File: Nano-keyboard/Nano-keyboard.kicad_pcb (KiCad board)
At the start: 2 copper layers, 120 x 77 mm, 42 parts, among them J1 125SH-B-04-TS, J2 125SH-B-02-TS, U1 AMS1117, U2 ESP32-WROOM-32, U3 J5019, U5 EN12-HN22AF25, U6 EN12-HN22AF25

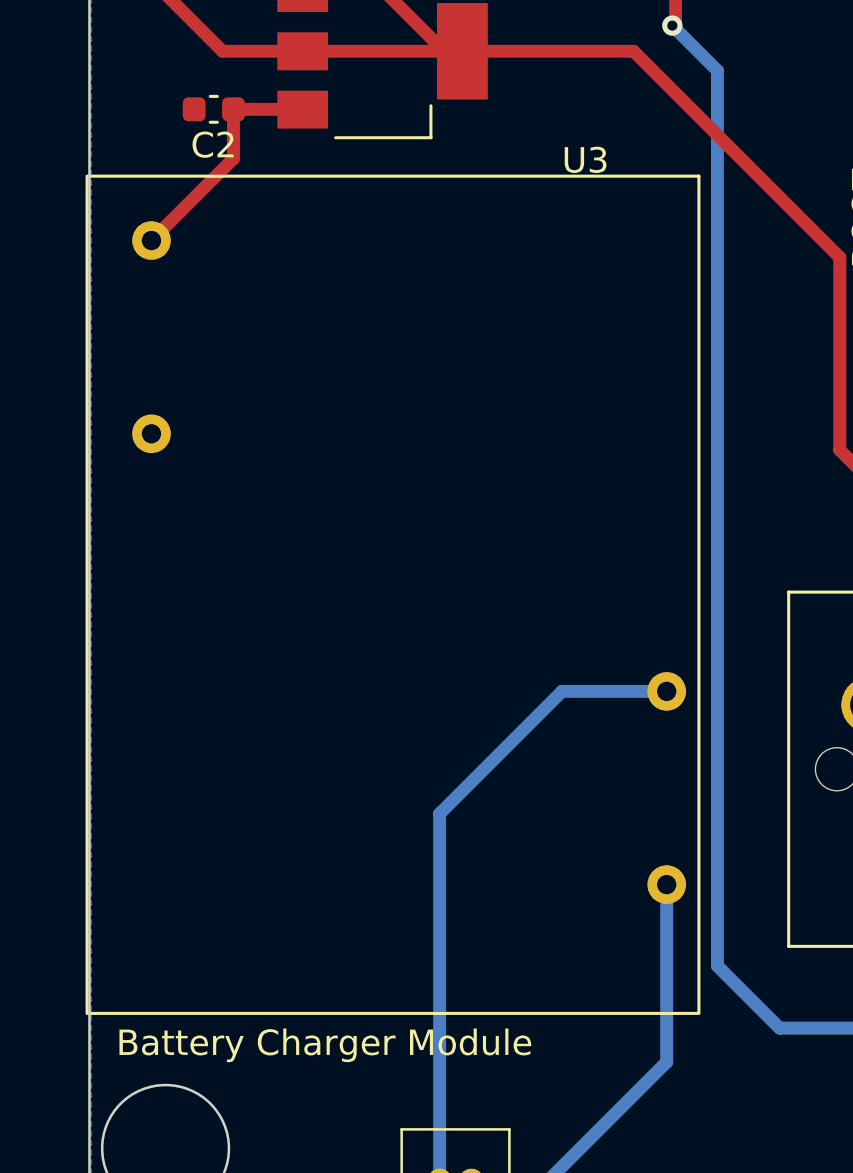
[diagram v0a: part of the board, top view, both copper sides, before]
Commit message: Footprint adjustmetns
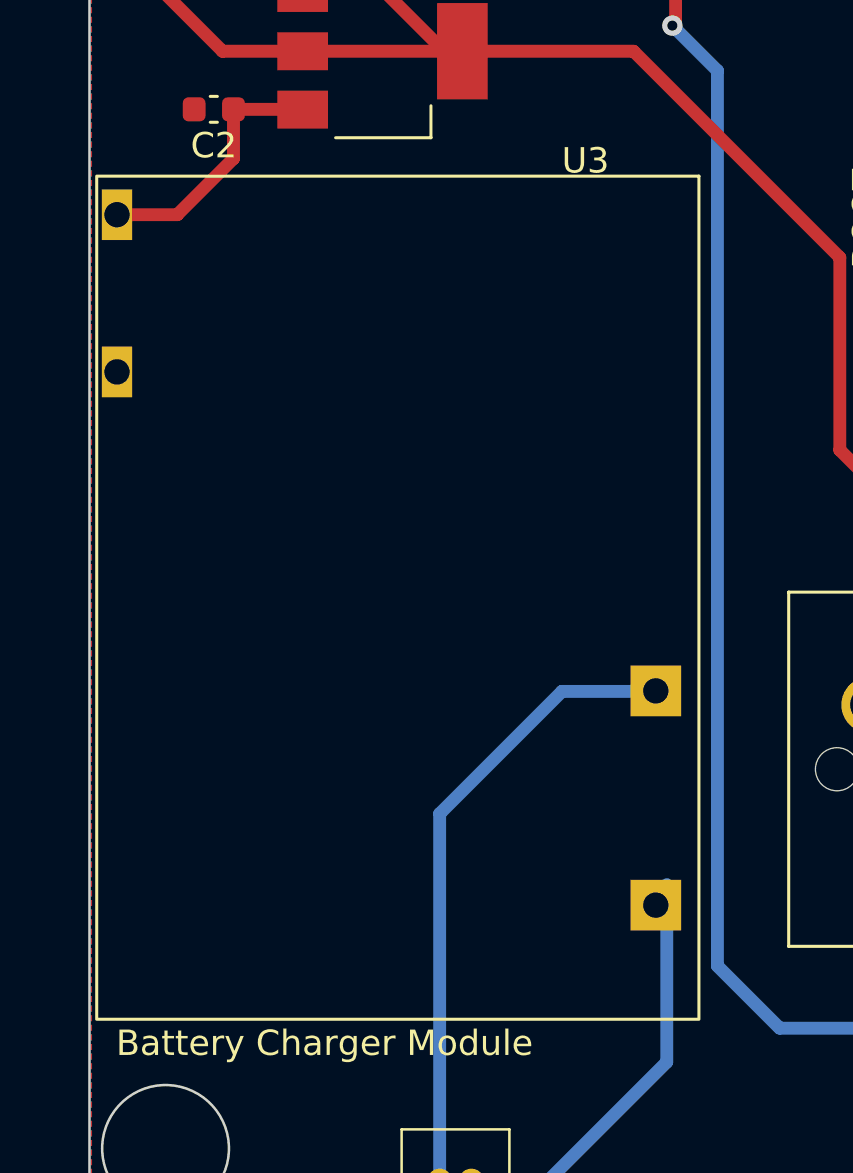
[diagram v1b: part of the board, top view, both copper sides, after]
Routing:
- net Net-(C2-Pad1): track 9.25 -> 10.2 mm
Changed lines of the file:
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@@
       (effects (font (size 1 1) (thickness 0.15)))
     )
-    (fp_rect (start 0 0) (end 33.02 24.13) (layer "F.SilkS") (width 0.12) (fill none))
-    (pad "1" thru_hole circle (at 20.32 1.27 270) (size 1.524 1.524) (drill 0.762) (layers *.Cu *.Mask)
+    (fp_rect (start 0 0) (end 33.25 23.75) (layer "F.SilkS") (width 0.12) (fill none))
+    (pad "1" thru_hole rect (at 20.3 1.7 270) (size 2 2) (drill 1) (layers *.Cu *.Mask)
       (net 49 "Net-(J2-Pad1)") (pinfunction "BAT+") (pintype "input"))
-    (pad "2" thru_hole circle (at 27.94 1.27 270) (size 1.524 1.524) (drill 0.762) (layers *.Cu *.Mask)
+    (pad "2" thru_hole rect (at 28.75 1.7 270) (size 2 2) (drill 1) (layers *.Cu *.Mask)
       (net 50 "Net-(J2-Pad2)") (pinfunction "BAT-") (pintype "input"))
-    (pad "3" thru_hole circle (at 2.54 21.59 270) (size 1.524 1.524) (drill 0.762) (layers *.Cu *.Mask)
+    (pad "3" thru_hole rect (at 1.52 22.95 270) (size 2 1.2) (drill 1) (layers *.Cu *.Mask)
       (net 43 "Net-(C2-Pad1)") (pinfunction "VOUT+") (pintype "input"))
-    (pad "4" thru_hole circle (at 10.16 21.59 270) (size 1.524 1.524) (drill 0.762) (layers *.Cu *.Mask)
+    (pad "4" thru_hole rect (at 7.72 22.95 270) (size 2 1.2) (drill 1) (layers *.Cu *.Mask)
       (net 1 "GND") (pinfunction "VOUT-") (pintype "input"))
+    (zone (net 0) (net_name "") (layer "F.Cu") (name "Keep out Module") (hatch full 0.508)
+      (connect_pads (clearance 0))
+      (min_thickness 0.254)
+      (keepout (tracks allowed) (vias not_allowed) (pads not_allowed ) (copperpour not_allowed) (footprints not_allowed))
+      (fill (thermal_gap 0.508) (thermal_bridge_width 0.508))
+      (polygon
+        (pts
+          (xy 66.96 133.675)
+          (xy 66.988006 111.119522)
+          (xy 68.89336 111.134836)
+          (xy 68.865354 105.762314)
+          (xy 66.961 105.759)
+          (xy 66.96 100.425)
+          (xy 90.71 100.425)
+          (xy 90.71 133.675)
+        )
+      )
+    )
   )
   (footprint "lib:SW_Cherry_MX_1.00u_PCB" (layer "F.Cu")
@@
   (segment (start 87.884 89.662) (end 90.678 86.868) (width 0.508) (layer "B.Cu") (net 31))
   (segment (start 130.302 82.55) (end 130.302 77.978) (width 0.508) (layer "B.Cu") (net 31))
-  (segment (start 72.353 99.732) (end 69.12 102.965) (width 0.508) (layer "F.Cu") (net 43))
   (segment (start 72.353 97.79) (end 75.072 97.79) (width 0.508) (layer "F.Cu") (net 43))
+  (segment (start 70.14 101.945) (end 72.353 99.732) (width 0.508) (layer "F.Cu") (net 43))
+  (segment (start 67.76 101.945) (end 70.14 101.945) (width 0.508) (layer "F.Cu") (net 43))
   (segment (start 72.353 97.79) (end 72.353 99.732) (width 0.508) (layer "F.Cu") (net 43))
   (segment (start 75.072 97.79) (end 75.082 97.8) (width 0.508) (layer "F.Cu") (net 43))

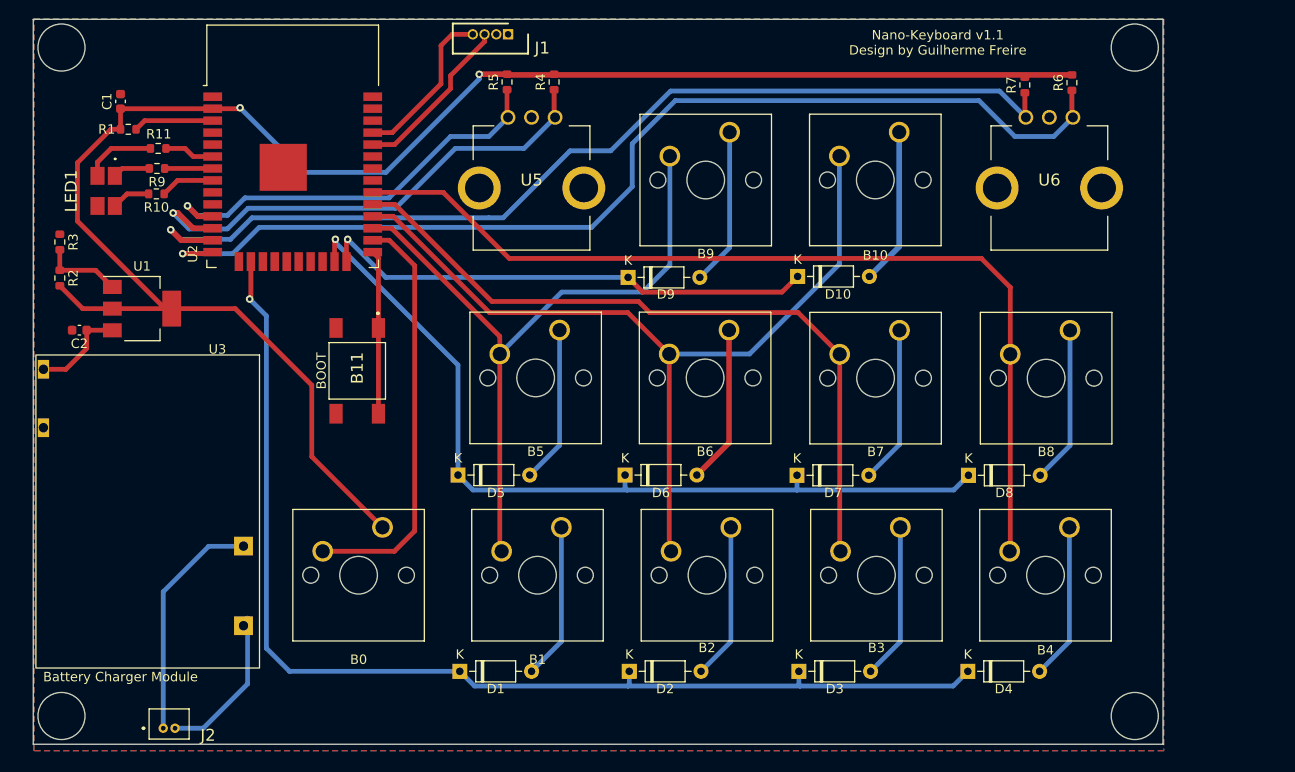
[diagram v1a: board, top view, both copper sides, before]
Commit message: Adjusting J5019 footprint
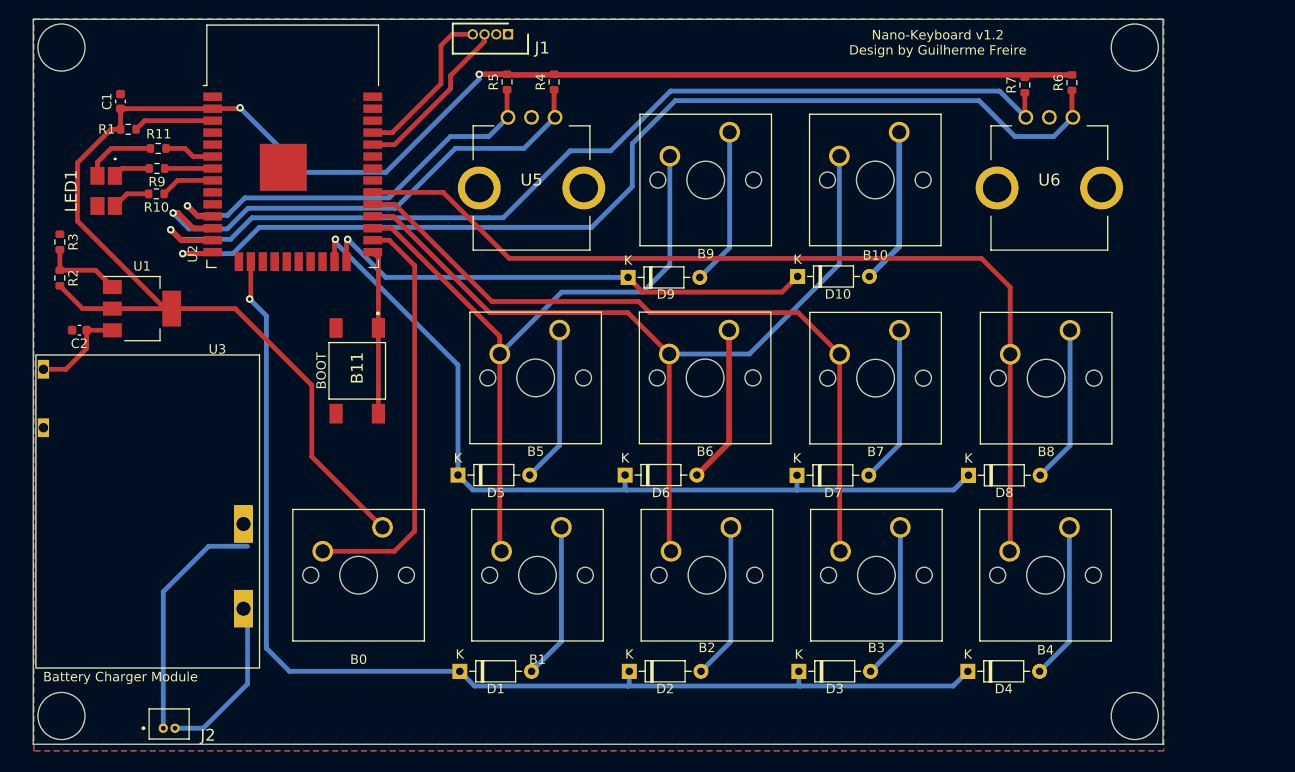
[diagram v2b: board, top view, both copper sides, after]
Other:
- board text added: "Nano-Keyboard v1.2 Design by Guilherme Freire"
- board text removed: "Nano-Keyboard v1.1 Design by Guilherme Freire"
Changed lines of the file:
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@@
     )
     (fp_rect (start 0 0) (end 33.25 23.75) (layer "F.SilkS") (width 0.12) (fill none))
-    (pad "1" thru_hole rect (at 20.3 1.7 270) (size 2 2) (drill 1) (layers *.Cu *.Mask)
+    (pad "1" thru_hole rect (at 17.95 1.7 270) (size 4 2) (drill 1.5) (layers *.Cu *.Mask)
       (net 49 "Net-(J2-Pad1)") (pinfunction "BAT+") (pintype "input"))
-    (pad "2" thru_hole rect (at 28.75 1.7 270) (size 2 2) (drill 1) (layers *.Cu *.Mask)
+    (pad "2" thru_hole rect (at 26.95 1.7 270) (size 4 2) (drill 1.5) (layers *.Cu *.Mask)
       (net 50 "Net-(J2-Pad2)") (pinfunction "BAT-") (pintype "input"))
     (pad "3" thru_hole rect (at 1.52 22.95 270) (size 2 1.2) (drill 1) (layers *.Cu *.Mask)
@@
           (xy 66.96 133.675)
           (xy 66.988006 111.119522)
-          (xy 68.89336 111.134836)
-          (xy 68.865354 105.762314)
+          (xy 66.980465 111.144809)
+          (xy 66.952459 105.772287)
           (xy 66.961 105.759)
           (xy 66.96 100.425)
@@
     (effects (font (size 1 1) (thickness 0.15)) (justify mirror))
   )
-  (gr_text "Nano-Keyboard v1.1\nDesign by Guilherme Freire\n" (at 162.749992 67.250005) (layer "F.SilkS")
+  (gr_text "Nano-Keyboard v1.2\nDesign by Guilherme Freire\n" (at 162.749992 67.250005) (layer "F.SilkS")
     (effects (font (size 1 1) (thickness 0.2)))
   )

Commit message: Update
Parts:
- U3: moved to B.Cu
- moved U3 32.7 mm to (90.9, 133.1), turned to 90 degrees
- moved B10 12.8 mm to (160.0, 89.5), turned to 180 degrees
- moved B9 12.7 mm to (140.0, 89.5), turned to 180 degrees
- moved B8 12.1 mm to (180.0, 109.5), turned to 180 degrees
- moved B5 12.0 mm to (120.0, 109.5), turned to 180 degrees
- moved B7 11.7 mm to (160.0, 109.5), turned to 180 degrees
- moved B6 11.7 mm to (140.0, 109.5), turned to 180 degrees
- moved B0 11.4 mm to (100.0, 129.5), turned to 180 degrees
- moved B4 11.2 mm to (180.0, 129.5), turned to 180 degrees
- moved B1 11.1 mm to (120.0, 129.5), turned to 180 degrees
- moved U6 11.0 mm to (187.9, 77.1)
- moved B3 10.8 mm to (160.0, 129.5), turned to 180 degrees
- moved B2 10.8 mm to (140.0, 129.5), turned to 180 degrees
- moved D4 9.79 mm to (175.7, 133.3)
- moved D8 9.70 mm to (175.7, 113.1)
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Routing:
- net +3V3: track 186.2 -> 0.00 mm, vias 2 -> 0
- net ROW1: track 121.9 -> 0.00 mm, vias 1 -> 0
- net /ENCODER1_A: track 112.5 -> 0.00 mm, vias 1 -> 0
- net /ENCODER1_B: track 106.5 -> 0.00 mm, vias 1 -> 0
- net COL4: track 100.0 -> 0.00 mm
- net COL2: track 92.1 -> 0.00 mm
- net ROW2: track 91.7 -> 0.00 mm, vias 1 -> 0
- net COL3: track 77.2 -> 0.00 mm
- net COL1: track 74.7 -> 0.00 mm
- net /ENCODER2_A: track 54.0 -> 0.00 mm, vias 1 -> 0
- net ROW3: track 53.2 -> 0.00 mm, vias 1 -> 0
- net /ENCODER2_B: track 44.9 -> 0.00 mm, vias 1 -> 0
- net /FUNC: track 44.4 -> 0.00 mm
- net Net-(J2-Pad1): track 25.5 -> 0.00 mm
- net /RX0: track 18.0 -> 0.00 mm
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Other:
- board size 120 x 77 mm -> 130 x 77 mm
- board text added: "NANO KEYBOARD"

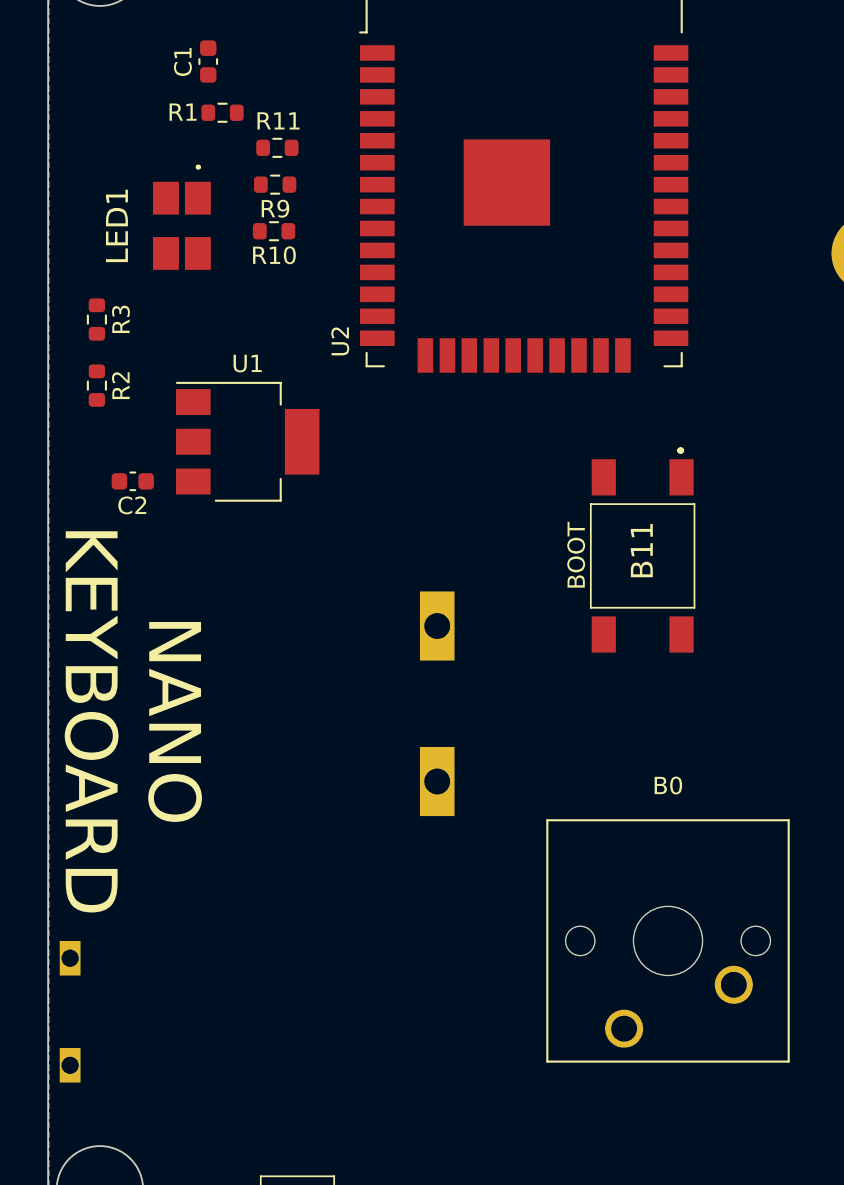
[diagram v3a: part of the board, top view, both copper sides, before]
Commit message: added BJTs
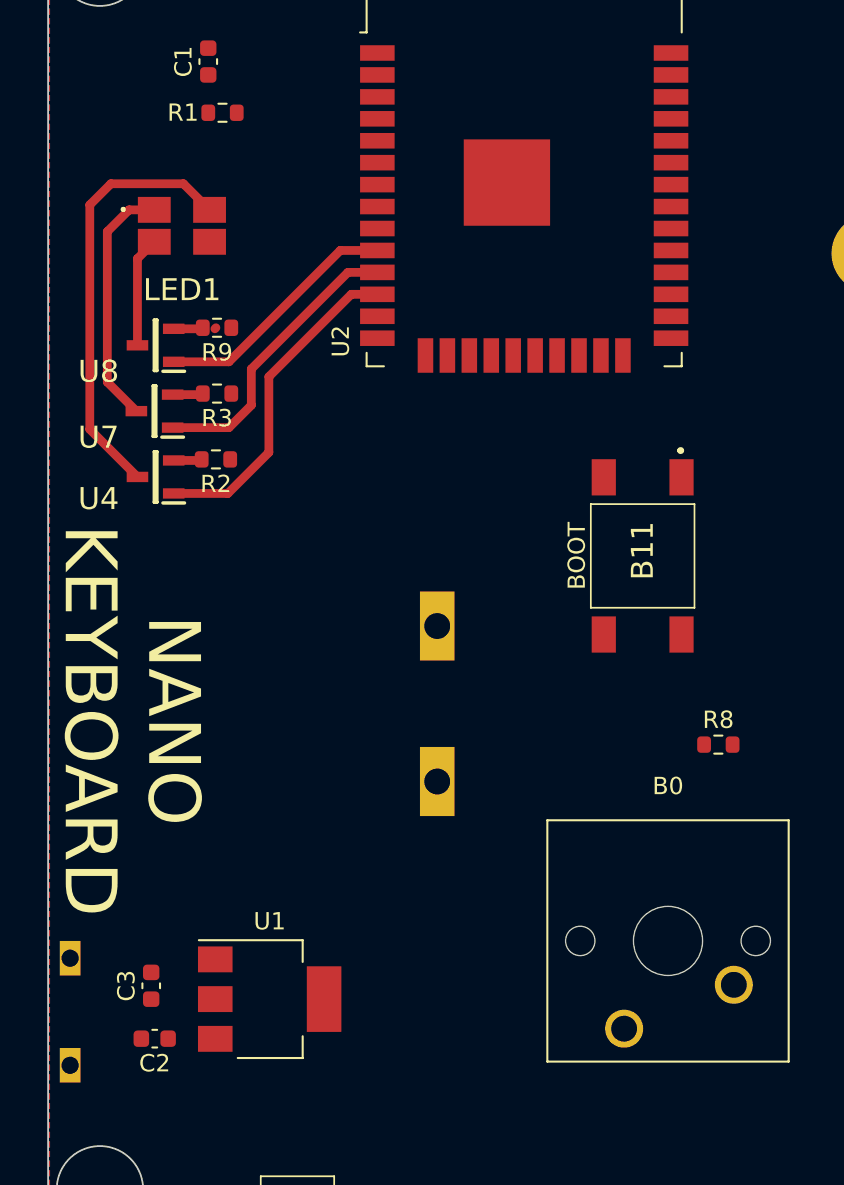
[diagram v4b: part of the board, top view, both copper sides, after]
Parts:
- removed R10, R11: R_0603, lib:R_0603_1608Metric
- added C3: C_0603, lib:C_0603_1608Metric, F.Cu at (72.6, 127.0)
- added R8: R_0603, lib:R_0603_1608Metric, F.Cu at (105.5, 113.0)
- added U4: QBC847BL, lib:SOT96P237X111-3N, F.Cu at (72.9, 97.5)
- added U7: QBC847BL, lib:SOT96P237X111-3N, F.Cu at (72.8, 93.7)
- added U8: QBC847BL, lib:SOT96P237X111-3N, F.Cu at (72.9, 89.9)
- moved U1 32.3 mm to (79.5, 127.8)
- moved C2 32.3 mm to (72.8, 130.1)
- moved R9 8.94 mm to (76.5, 88.9)
- moved R3 8.17 mm to (76.5, 92.7), turned to 180 degrees
- moved R2 8.11 mm to (76.4, 96.5), turned to 180 degrees
- turned LED1 to 0 degrees
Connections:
- LED1 pad 1: Net-(LED1-Pad1) -> /KG
- LED1 pad 2: Net-(LED1-Pad2) -> /KR
- LED1 pad 3: Net-(LED1-Pad3) -> /KB
- LED1 pad 4: GND -> +3V3
- R2 pad 1: Net-(R2-Pad1) -> GND
- R2 pad 2: +3V3 -> Net-(R2-Pad2)
- R3 pad 2: Net-(R2-Pad1) -> Net-(R3-Pad2)
- R9 pad 1: /LED_GREEN -> GND
- R9 pad 2: Net-(LED1-Pad1) -> Net-(R9-Pad2)
- U1 pad 1: Net-(R2-Pad1) -> GND
- U2 pad 10: unconnected-(U2-Pad10) -> /LED_BLUE
- U2 pad 11: /ENCODER2_B -> /LED_GREEN
- U2 pad 12: /ENCODER2_A -> /LED_RED
- U2 pad 13: /ENCODER1_B -> unconnected-(U2-Pad13)
- U2 pad 14: /ENCODER1_A -> unconnected-(U2-Pad14)
- U2 pad 16: ROW1 -> unconnected-(U2-Pad16)
- U2 pad 23: ROW2 -> unconnected-(U2-Pad23)
- U2 pad 24: ROW3 -> /FUNC
- U2 pad 26: /FUNC -> COL1
- U2 pad 27: COL1 -> COL2
- U2 pad 28: COL2 -> COL3
- U2 pad 29: COL3 -> unconnected-(U2-Pad29)
- U2 pad 31: unconnected-(U2-Pad31) -> /ENCODER2_B
- U2 pad 33: unconnected-(U2-Pad33) -> /ENCODER2_A
- U2 pad 36: unconnected-(U2-Pad36) -> /ENCODER1_B
- U2 pad 37: unconnected-(U2-Pad37) -> /ENCODER1_A
- U2 pad 6: /LED_BLUE -> ROW3
- U2 pad 7: /LED_GREEN -> unconnected-(U2-Pad7)
- U2 pad 8: /LED_RED -> ROW1
- U2 pad 9: unconnected-(U2-Pad9) -> ROW2
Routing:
- net /KR: track 0.00 -> 25.0 mm
- net /LED_RED: track 0.00 -> 19.1 mm
- net /LED_GREEN: track 0.00 -> 16.8 mm
- net /LED_BLUE: track 0.00 -> 14.5 mm
- net /KG: track 0.00 -> 14.3 mm
- net /KB: track 0.00 -> 6.39 mm
- net Net-(R9-Pad2): track 0.00 -> 1.79 mm
- net Net-(R3-Pad2): track 0.00 -> 1.77 mm
- net Net-(R2-Pad2): track 0.00 -> 1.64 mm
